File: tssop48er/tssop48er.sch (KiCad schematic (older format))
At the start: 32 parts

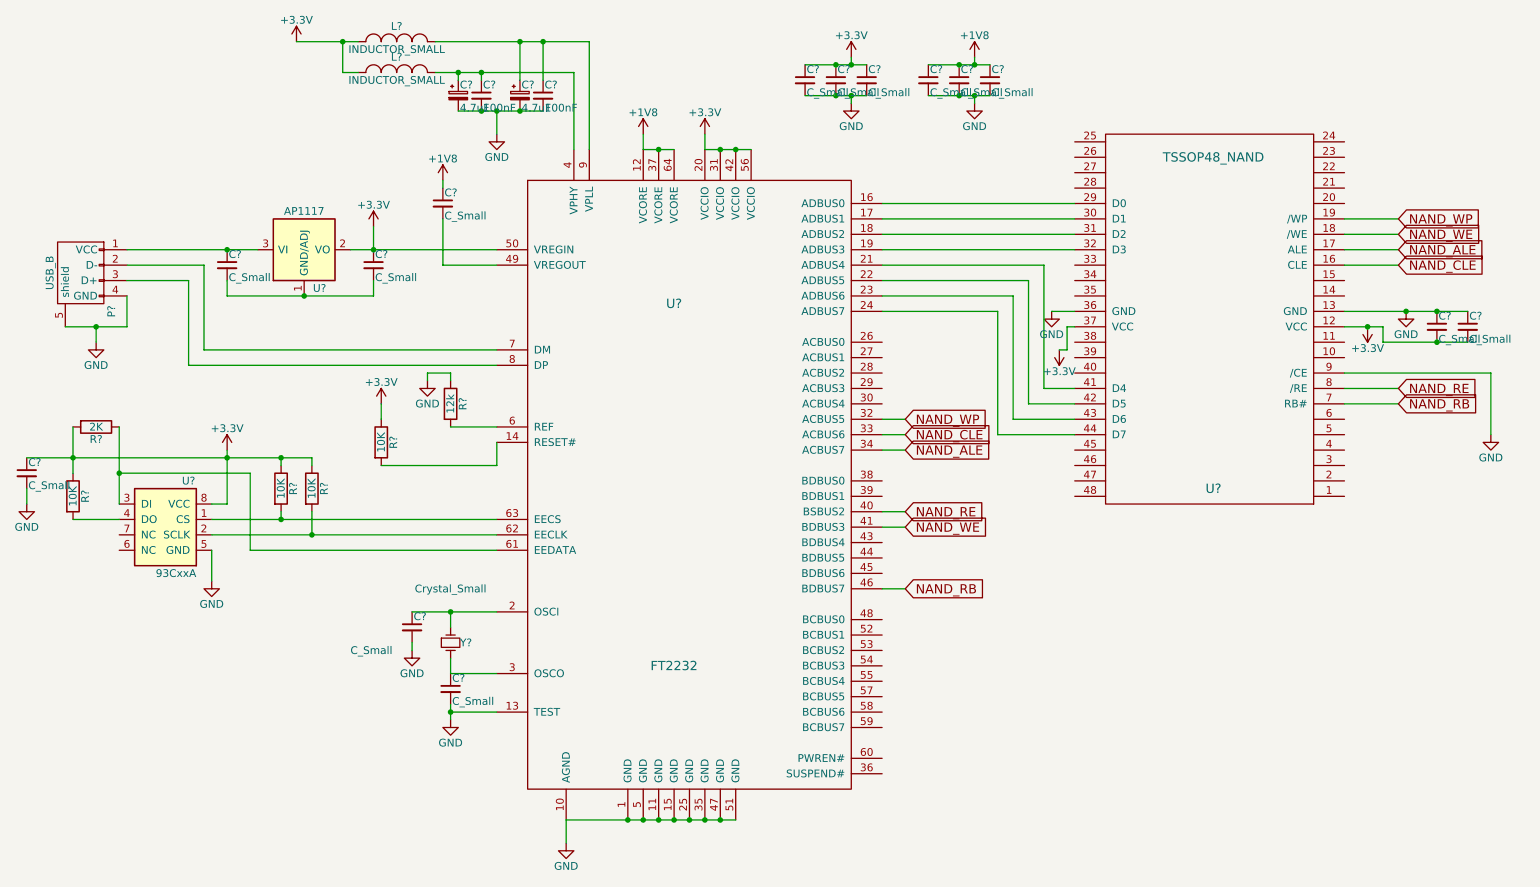
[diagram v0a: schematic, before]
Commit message: Adding missing boards/reorged
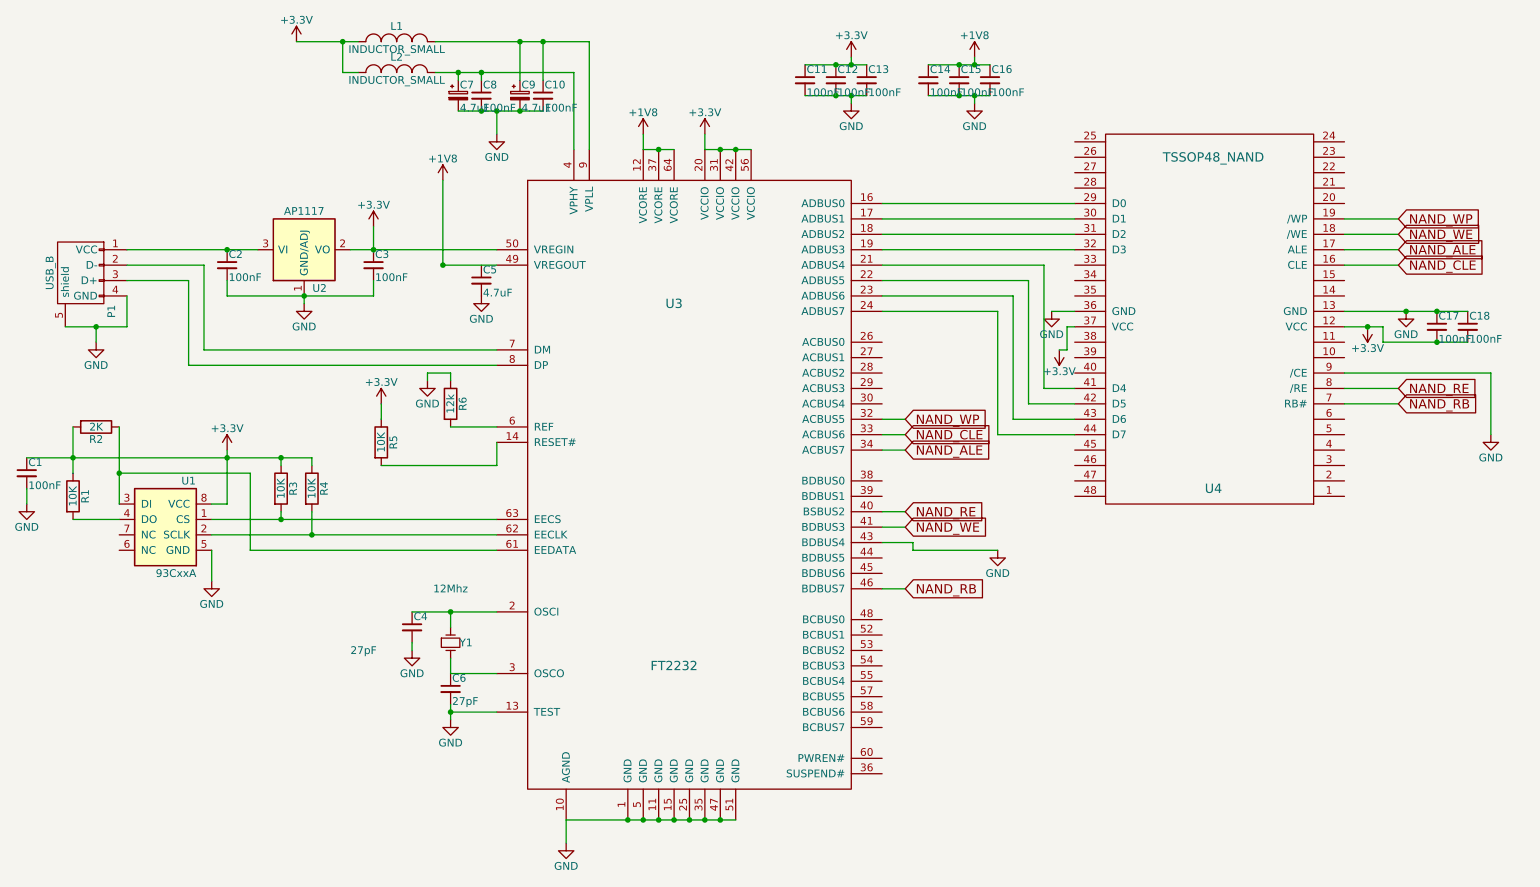
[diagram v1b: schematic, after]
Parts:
- C1, C11, C12, C13, C14, C15, C16, C17, C18, C2, C3: renamed from C?; value C_Small -> 100nF; footprint (none) -> Capacitors_SMD:C_0805_HandSoldering
- C10, C8: renamed from C?; footprint (none) -> Capacitors_SMD:C_0805_HandSoldering
- C4, C6: renamed from C?; value C_Small -> 27pF; footprint (none) -> Capacitors_SMD:C_0805_HandSoldering
- C5: renamed from C?; value C_Small -> 4.7uF; footprint (none) -> Capacitors_SMD:C_0805_HandSoldering
- C7, C9: renamed from C?; footprint (none) -> Capacitors_SMD:c_elec_4x5.3
- L1, L2: renamed from L?; footprint (none) -> Capacitors_SMD:C_0805_HandSoldering
- P1: renamed from P?; footprint (none) -> usbAtaobao:USB_A
- R1, R2, R3, R4, R5, R6: renamed from R?; footprint (none) -> Capacitors_SMD:C_0805_HandSoldering
- U1: renamed from U?; footprint (none) -> Housings_SOIC:SOIC-8_3.9x4.9mm_Pitch1.27mm
- U2: renamed from U?; footprint (none) -> TO_SOT_Packages_SMD:SOT-223
- U3: renamed from U?; footprint (none) -> Housings_QFP:LQFP-64_14x14mm_Pitch0.8mm
- U4: renamed from U?; footprint (none) -> tsop48zif:TSOP48ZIF
- Y1: renamed from Y?; value Crystal_Small -> 12Mhz; footprint (none) -> Crystals:HC-49V
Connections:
- net +1V8: now also U3.49 (VREGOUT); no longer C5.1
- net GND: now also C2.2, C3.2, C5.2, U2.1 (GND/ADJ), U3.43 (BDBUS4)
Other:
- moved on the sheet: C5
